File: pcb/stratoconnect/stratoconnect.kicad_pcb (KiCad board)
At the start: 4 copper layers, 72.2 x 46 mm, 49 parts, among them J1 Conn_Coaxial, J2 Conn_02x03_Odd_Even, J3 Conn_01x05_Male, J4 Conn_01x02_Male, J5 Conn_01x03_Male, SW1 SW_SPST, SW2 SW_SPST, U1 RF4463f30, U2 ATmega328PB-A, U3 TPS61022RWU, U4 PCA9306DC, Y1 CSTNE16M0V530000R0

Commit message: add bom, readjust capactor annotations
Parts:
- C1, C4: value 4.7uF -> 100n
- C10: value 100nF -> 1u
- C2, C3: value 1uF -> 1u
- C6, C9: value 100nF -> 100n
- C7, C8: value 47uF -> 47u
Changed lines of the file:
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@@
       (drillshape 0)
       (scaleselection 1)
-      (outputdirectory "/Users/kevinlutzer/Projects/StratoConnect/fab")
+      (outputdirectory "/Users/kevinlutzer/Projects/StratoConnect/fab/gerbers_v1")
     )
   )
@@
       (effects (font (size 1 1) (thickness 0.15)))
     )
-    (fp_text value "47uF" (at 0 3.7 90) (layer "F.Fab") hide
+    (fp_text value "47u" (at 0 3.7 90) (layer "F.Fab") hide
       (effects (font (size 1 1) (thickness 0.15)))
     )
@@
       (effects (font (size 1 1) (thickness 0.15)))
     )
-    (fp_text value "4.7uF" (at 0 1.43) (layer "F.Fab") hide
+    (fp_text value "100n" (at 0 1.43) (layer "F.Fab") hide
       (effects (font (size 1 1) (thickness 0.15)))
     )
@@
       (effects (font (size 1 1) (thickness 0.15)))
     )
-    (fp_text value "4.7uF" (at 0 1.43) (layer "F.Fab") hide
+    (fp_text value "100n" (at 0 1.43) (layer "F.Fab") hide
       (effects (font (size 1 1) (thickness 0.15)))
     )
@@
       (effects (font (size 1 1) (thickness 0.15)))
     )
-    (fp_text value "47uF" (at 0 3.7 90) (layer "F.Fab") hide
+    (fp_text value "47u" (at 0 3.7 90) (layer "F.Fab") hide
       (effects (font (size 1 1) (thickness 0.15)))
     )
@@
       (effects (font (size 1 1) (thickness 0.15)))
     )
-    (fp_text value "100nF" (at 0 1.43) (layer "F.Fab") hide
+    (fp_text value "1u" (at 0 1.43) (layer "F.Fab") hide
       (effects (font (size 1 1) (thickness 0.15)))
     )
@@
       (effects (font (size 1 1) (thickness 0.15)))
     )
-    (fp_text value "1uF" (at 0 1.43 90) (layer "F.Fab") hide
+    (fp_text value "1u" (at 0 1.43 90) (layer "F.Fab") hide
       (effects (font (size 1 1) (thickness 0.15)))
     )
@@
       (effects (font (size 1 1) (thickness 0.15)))
     )
-    (fp_text value "100nF" (at 0 1.43 90) (layer "F.Fab") hide
+    (fp_text value "100n" (at 0 1.43 90) (layer "F.Fab") hide
       (effects (font (size 1 1) (thickness 0.15)))
     )
@@
       (effects (font (size 1 1) (thickness 0.15)))
     )
-    (fp_text value "1uF" (at 0 1.43) (layer "F.Fab") hide
+    (fp_text value "1u" (at 0 1.43) (layer "F.Fab") hide
       (effects (font (size 1 1) (thickness 0.15)))
     )
@@
       (effects (font (size 1 1) (thickness 0.15)))
     )
-    (fp_text value "100nF" (at 0 1.43) (layer "F.Fab") hide
+    (fp_text value "100n" (at 0 1.43) (layer "F.Fab") hide
       (effects (font (size 1 1) (thickness 0.15)))
     )

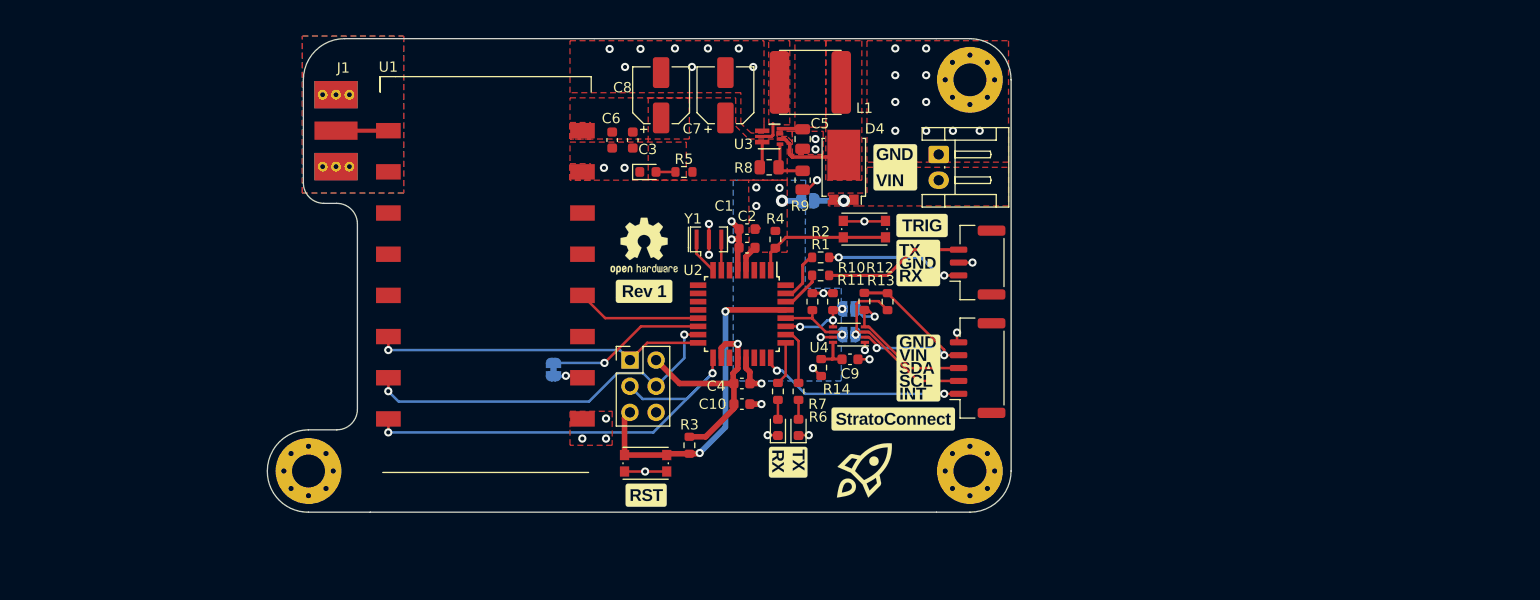
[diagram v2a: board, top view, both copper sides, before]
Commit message: add labels update rf lib
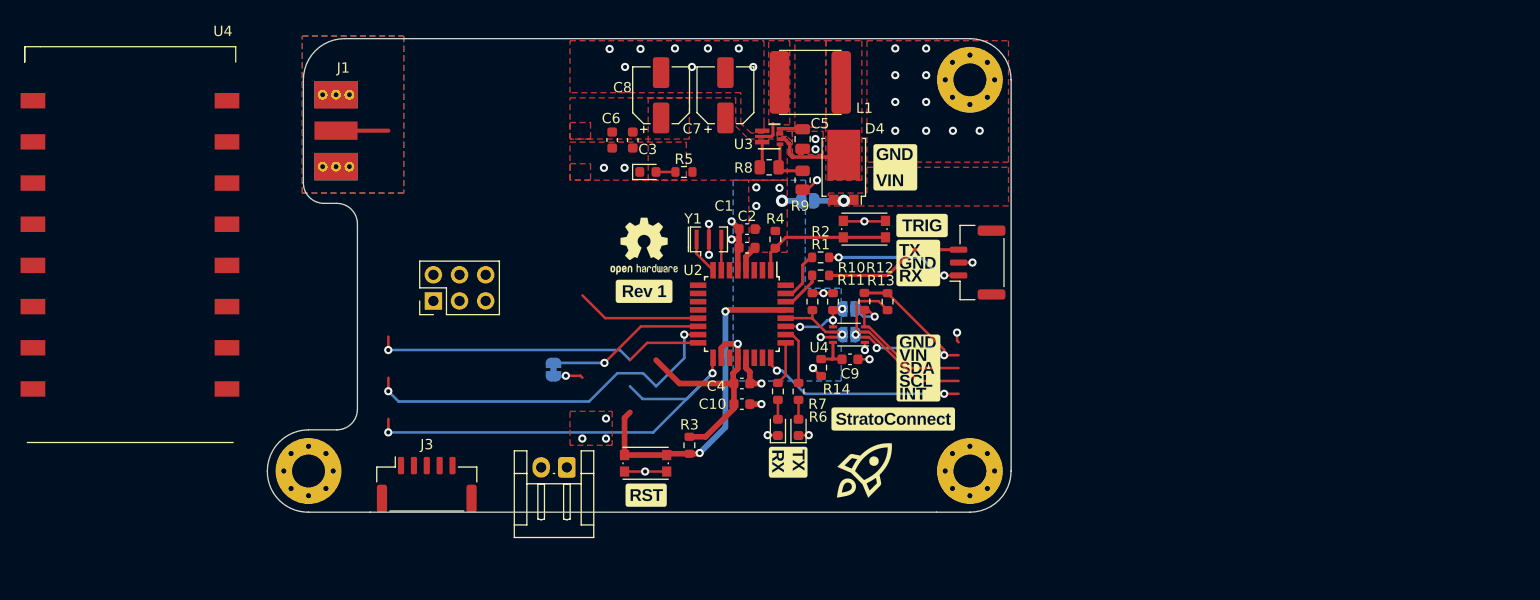
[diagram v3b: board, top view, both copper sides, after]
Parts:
- removed U1: RF4463f30, RF:RF4463F30
- added U4: RF4463F30, Kevin_Lutzer_Lbr:RF4463F30, F.Cu at (122.7, 67.3)
- moved J3 54.7 mm to (151.5, 90.6), turned to 0 degrees
- moved J4 47.2 mm to (165.1, 88.9), turned to 180 degrees
- moved J2 19.9 mm to (152.1, 72.7), turned to 90 degrees
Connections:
- net /LED_RX renamed LED_RX
- net /LED_TX renamed LED_TX
- net /SPI_MISO renamed SPI_MISO
- net /SPI_MOSI renamed SPI_MOSI
- net /SPI_SCK renamed SPI_SCK
- net /TRIG renamed ~{TRIG}
- net /UART_RX renamed UART_RX
- net /UART_TX renamed UART_TX
- net /~{INT} renamed ~{INT}
- net /~{IRQ} renamed ~{IRQ}
- net /~{RST} renamed ~{RST}
- J3 pad 2: /SCL_LVL -> SCL_LVL
- J3 pad 3: /SDA_LVL -> SDA_LVL
- J3 pad 4: +3V3 -> +5V
- U2 pad 13: /~{SDN} -> ~{SDN}
- U2 pad 14: /~{SPI_CS} -> ~{SPI_CS}
- U2 pad 27: /SDA -> SDA
- U2 pad 28: /SCL -> SCL
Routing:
- net ~{SDN}: track 0.00 -> 12.2 mm
- net /~{SDN}: track 12.2 -> 0.00 mm

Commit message: WIP
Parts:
- removed J3: Conn_01x05_Male, Connector_JST:JST_GH_SM05B-GHS-TB_1x05-1MP_P1.25mm_Horizontal
- removed J4: Conn_01x02_Male, Connector_JST:JST_EH_S2B-EH_1x02_P2.50mm_Horizontal
- removed J5: Conn_01x03_Male, Connector_JST:JST_GH_SM03B-GHS-TB_1x03-1MP_P1.25mm_Horizontal
- removed JP1: SolderJumper_2_Bridged, Jumper:SolderJumper-2_P1.3mm_Bridged_RoundedPad1.0x1.5mm
- removed JP3, JP4: SolderJumper_2_Open, Jumper:SolderJumper-2_P1.3mm_Open_RoundedPad1.0x1.5mm
- removed R12, R13: 22k, Resistor_SMD:R_0603_1608Metric
- removed R14: 10k, Resistor_SMD:R_0603_1608Metric
- removed REF**: OSHW-Logo2_7.3x6mm_SilkScreen, Symbol:OSHW-Logo2_7.3x6mm_SilkScreen
- removed U3: TPS61022RWU, Package_DFN_QFN:VDFN-7_2.1x2.1mm
- removed the U4 at (122.7, 67.3)
- removed the U4 at (192.5, 76.0)
- added C11: 33p, Capacitor_SMD:CP_Elec_5x5.3, F.Cu at (238.9, 72.8)
- added U1: TPS565242, Package_TO_SOT_SMD:SOT-563, F.Cu at (256.4, 77.8)
- added U4: RF4463F30, Kevin_Lutzer_Lbr:RF4463F30, B.Cu at (159.3, 77.8)
- C9: footprint Capacitor_SMD:C_0603_1608Metric -> Capacitor_SMD:CP_Elec_5x5.3
- J1: footprint Connector_Coaxial:SMA_Molex_73251-2120_EdgeMount_Horizontal -> Connector_Coaxial:SMA_Amphenol_901-143_Horizontal
- JP2: moved to F.Cu
- L1: value 1u -> L; footprint Inductor_SMD:L_2440_6060Metric -> Inductor_SMD_Wurth:L_Wurth_WE-LQSH-4020
- R10: value 22k -> 100k; footprint Resistor_SMD:R_0603_1608Metric -> Resistor_SMD:R_0805_2012Metric
- R11: value 22k -> 25.5k; footprint Resistor_SMD:R_0603_1608Metric -> Resistor_SMD:R_0805_2012Metric
- R8: value 732k -> 158k
- R9: value 100k -> 30k
- moved H2 111.1 mm to (247.4, 60.7)
- moved J2 103.8 mm to (253.7, 51.1), turned to 0 degrees
- moved C6 79.1 mm to (236.4, 99.2), turned to 0 degrees
- moved C3 74.8 mm to (236.4, 94.2), turned to 0 degrees
- moved R5 73.9 mm to (244.5, 89.2), turned to 0 degrees
- moved U2 72.9 mm to (252.3, 93.7), turned to 0 degrees
- moved R8 68.8 mm to (253.5, 60.0)
- moved D1 66.1 mm to (231.4, 91.1)
- moved JP2 65.6 mm to (253.5, 72.1)
- moved R9 65.6 mm to (253.5, 62.9), turned to 0 degrees
- moved C8 65.0 mm to (238.9, 59.1), turned to 0 degrees
- moved R10 65.0 mm to (253.5, 65.9), turned to 0 degrees
- moved R3 64.2 mm to (240.4, 96.7), turned to 0 degrees
- moved R4 63.9 mm to (240.4, 99.2), turned to 0 degrees
- moved R11 62.7 mm to (253.5, 68.8), turned to 0 degrees
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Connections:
- net Net-(U3-FB) renamed /FB
- C5 pad 1: /VDC_FWD -> Net-(D4-K)
- C9 pad 1: Net-(U4-EN) -> /SW
- C9 pad 2: GND -> Net-(U1-VBST)
- D4 pad 1: /VDC_FWD -> Net-(D4-K)
- L1 pad 1: /VDC_FWD -> /SW
- L1 pad 2: /SW -> +5V
- R10 pad 1: +5V -> Net-(D4-K)
- R10 pad 2: /SCL -> /EN
- R11 pad 1: +5V -> /EN
- R11 pad 2: /SDA -> GND
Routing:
- net SPI_SCK: track 46.3 -> 0.00 mm, vias 2 -> 0
- net SPI_MOSI: track 36.9 -> 0.00 mm, vias 2 -> 0
- net +5V: track 34.8 -> 0.00 mm, vias 8 -> 0
- net SPI_MISO: track 32.5 -> 0.00 mm, vias 1 -> 0
- net ~{RST}: track 32.4 -> 0.00 mm, vias 2 -> 0
- net GND: track 29.9 -> 0.00 mm, vias 40 -> 0
- net +3V3: track 20.6 -> 0.00 mm, vias 2 -> 0
- net ~{INT}: track 20.1 -> 0.00 mm, vias 2 -> 0
- net /SCL_LVL: track 18.3 -> 0.00 mm, vias 1 -> 0
- net /SDA_LVL: track 15.9 -> 0.00 mm, vias 1 -> 0
- net /~{SPI_CS}: track 15.5 -> 0.00 mm, vias 1 -> 0
- net UART_RX: track 13.6 -> 0.00 mm
- net ~{TRIG}: track 13.5 -> 0.00 mm
- net UART_TX: track 13.3 -> 0.00 mm, vias 2 -> 0
- net ~{SDN}: track 12.2 -> 0.00 mm
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- removed copper zone on B.Cu, net +5V
- removed copper zone on F.Cu, net +5V
- removed copper zone on B.Cu, net /RF_GND
- removed copper zone on F.Cu, net /RF_GND
- removed copper zone on In1.Cu, net /RF_GND
- removed copper zone on In2.Cu, net /RF_GND
- removed copper zone on F.Cu, net /SW
- removed copper zone on F.Cu, net /VDC_FWD
- removed copper zone on F.Cu, net GND
- removed copper zone on In1.Cu, net GND
- removed copper zone on In2.Cu, net GND
- removed copper zone on F.Cu, net VDC
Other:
- board outline removed
- copper layers 4 -> 2
- board text removed: "For JLCPCB 7628 Coplanar Trace 0.5 mm for spacing 0.397 mm for trace width"
- board text removed: "Routed on 0,01mm Placed on 0.25mm"
